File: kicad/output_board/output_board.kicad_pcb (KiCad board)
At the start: 2 copper layers, 0 parts

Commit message: add draft output board
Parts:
- added C1: 22uF, Capacitor_SMD:C_0805_2012Metric, F.Cu at (121.0, 82.0)
- added C10: 220uF, Capacitor_THT:CP_Radial_D8.0mm_P3.50mm, F.Cu at (135.4, 80.0)
- added C11: 100nF, Capacitor_SMD:C_0603_1608Metric, F.Cu at (138.5, 77.0)
- added C12: 220uF, Capacitor_THT:CP_Radial_D8.0mm_P3.50mm, F.Cu at (135.4, 91.1)
- added C13: 100nF, Capacitor_SMD:C_0603_1608Metric, F.Cu at (138.5, 88.1)
- added C14: 220uF, Capacitor_THT:CP_Radial_D8.0mm_P3.50mm, F.Cu at (135.4, 113.4)
- added C15: 100nF, Capacitor_SMD:C_0603_1608Metric, F.Cu at (138.5, 110.4)
- added C2: 22uF, Capacitor_SMD:C_0805_2012Metric, F.Cu at (124.0, 82.0)
- added C3: 22uF, Capacitor_SMD:C_0805_2012Metric, F.Cu at (127.1, 82.0)
- added C4: 10nF, Capacitor_SMD:C_0603_1608Metric, F.Cu at (112.5, 75.0)
- added C5: 220uF, Capacitor_THT:CP_Radial_D8.0mm_P3.50mm, F.Cu at (106.9, 91.4)
- added C6: 1uF, Capacitor_SMD:C_0603_1608Metric, F.Cu at (112.9, 102.2)
- added C7: 100nF, Capacitor_SMD:C_0603_1608Metric, F.Cu at (112.9, 104.8)
- added C8: 220uF, Capacitor_THT:CP_Radial_D8.0mm_P3.50mm, F.Cu at (135.4, 102.3)
- added C9: 100nF, Capacitor_SMD:C_0603_1608Metric, F.Cu at (138.4, 99.2)
- added D1: SS34, Diode_SMD:D_SMA, F.Cu at (117.2, 75.9)
- added D2: SMAJ13A, Diode_SMD:D_SMA, F.Cu at (148.2, 102.7)
- added D3: BAV23CL, Package_TO_SOT_SMD:SOT-23-3, F.Cu at (153.9, 102.7)
- added D4: SMAJ13A, Diode_SMD:D_SMA, F.Cu at (148.2, 80.4)
- added D5: BAV23CL, Package_TO_SOT_SMD:SOT-23-3, F.Cu at (153.9, 80.4)
- added D6: SMAJ13A, Diode_SMD:D_SMA, F.Cu at (148.2, 91.5)
- added D7: BAV23CL, Package_TO_SOT_SMD:SOT-23-3, F.Cu at (153.9, 91.5)
- added D8: SMAJ13A, Diode_SMD:D_SMA, F.Cu at (148.2, 113.8)
- added D9: BAV23CL, Package_TO_SOT_SMD:SOT-23-3, F.Cu at (153.9, 113.8)
- added FID1: Fiducial, Fiducial:Fiducial_1mm_Mask2mm, F.Cu at (123.3, 74.5)
- added FID2: Fiducial, Fiducial:Fiducial_1mm_Mask2mm, F.Cu at (210.4, 94.2)
- added FID3: Fiducial, Fiducial:Fiducial_1mm_Mask2mm, F.Cu at (105.5, 112.0)
- added H1: MountingHole, MountingHole:MountingHole_2.2mm_M2, F.Cu at (184.3, 74.5)
- added H2: MountingHole, MountingHole:MountingHole_2.2mm_M2, F.Cu at (105.5, 117.7)
- added J1: DRV_PWR, Connector_PinHeader_2.54mm:PinHeader_1x05_P2.54mm_Vertical, B.Cu at (137.3, 74.5)
- added J2: DRV, Connector_PinHeader_2.54mm:PinHeader_2x08_P2.54mm_Vertical, B.Cu at (124.6, 117.7)
- added J3: CH_OUT, Connector_PinSocket_2.54mm:PinSocket_1x12_P2.54mm_Vertical, B.Cu at (170.3, 117.7)
- added L1: 15uH, SaawLib:L_CJIANG_FXL0630, F.Cu at (106.9, 76.7)
- added Q1: IRF9Z24NPBF, Package_TO_SOT_THT:TO-220-3_Vertical, F.Cu at (141.1, 100.4)
- added Q10: IRF9Z24NPBF, Package_TO_SOT_THT:TO-220-3_Vertical, F.Cu at (141.1, 111.6)
- added Q11: AO3400A, Package_TO_SOT_SMD:SOT-23, F.Cu at (154.0, 117.4)
- added Q12: AO3400A, Package_TO_SOT_SMD:SOT-23, F.Cu at (154.0, 110.2)
- added Q2: AO3400A, Package_TO_SOT_SMD:SOT-23, F.Cu at (153.9, 106.2)
- added Q3: AO3400A, Package_TO_SOT_SMD:SOT-23, F.Cu at (153.9, 99.1)
- added Q4: IRF9Z24NPBF, Package_TO_SOT_THT:TO-220-3_Vertical, F.Cu at (141.1, 78.2)
- added Q5: AO3400A, Package_TO_SOT_SMD:SOT-23, F.Cu at (154.0, 84.0)
- added Q6: AO3400A, Package_TO_SOT_SMD:SOT-23, F.Cu at (154.0, 76.9)
- added Q7: IRF9Z24NPBF, Package_TO_SOT_THT:TO-220-3_Vertical, F.Cu at (141.1, 89.3)
- added Q8: AO3400A, Package_TO_SOT_SMD:SOT-23, F.Cu at (154.0, 95.1)
- added Q9: AO3400A, Package_TO_SOT_SMD:SOT-23, F.Cu at (154.0, 88.0)
- added R1: 100k, Resistor_SMD:R_0603_1608Metric, F.Cu at (121.4, 100.8)
- added R10: 100k, Resistor_SMD:R_0603_1608Metric, F.Cu at (148.0, 99.1)
- added R11: 100, Resistor_SMD:R_0603_1608Metric, F.Cu at (150.6, 99.1)
- added R12: 10k, Resistor_SMD:R_0603_1608Metric, F.Cu at (109.0, 104.8)
- added R13: 10k, Resistor_SMD:R_0603_1608Metric, F.Cu at (109.0, 102.2)
- added R14: 2k, Resistor_SMD:R_0603_1608Metric, F.Cu at (138.5, 84.5)
- added R15: 1k, Resistor_SMD:R_0603_1608Metric, F.Cu at (135.4, 85.1)
- added R16: 100k, Resistor_SMD:R_0603_1608Metric, F.Cu at (148.0, 84.0)
- added R17: 100, Resistor_SMD:R_0603_1608Metric, F.Cu at (150.6, 84.0)
- added R18: 100k, Resistor_SMD:R_0603_1608Metric, F.Cu at (148.0, 76.9)
- added R19: 100, Resistor_SMD:R_0603_1608Metric, F.Cu at (150.6, 76.9)
- added R2: 10k, Resistor_SMD:R_0603_1608Metric, F.Cu at (109.7, 86.2)
- added R20: 10k, Resistor_SMD:R_0603_1608Metric, F.Cu at (110.2, 115.8)
- added R21: 10k, Resistor_SMD:R_0603_1608Metric, F.Cu at (110.2, 118.3)
- added R22: 2k, Resistor_SMD:R_0603_1608Metric, F.Cu at (138.5, 95.6)
- added R23: 1k, Resistor_SMD:R_0603_1608Metric, F.Cu at (135.4, 96.2)
- added R24: 100k, Resistor_SMD:R_0603_1608Metric, F.Cu at (148.0, 95.1)
- added R25: 100, Resistor_SMD:R_0603_1608Metric, F.Cu at (150.6, 95.1)
- added R26: 100k, Resistor_SMD:R_0603_1608Metric, F.Cu at (148.0, 88.0)
- added R27: 100, Resistor_SMD:R_0603_1608Metric, F.Cu at (150.6, 88.0)
- added R28: 10k, Resistor_SMD:R_0603_1608Metric, F.Cu at (115.7, 118.3)
- added R29: 10k, Resistor_SMD:R_0603_1608Metric, F.Cu at (115.7, 115.8)
- added R3: 1.5k, Resistor_SMD:R_0603_1608Metric, F.Cu at (113.3, 86.2)
- added R30: 2k, Resistor_SMD:R_0603_1608Metric, F.Cu at (138.5, 117.9)
- added R31: 1k, Resistor_SMD:R_0603_1608Metric, F.Cu at (135.4, 118.5)
- added R32: 100k, Resistor_SMD:R_0603_1608Metric, F.Cu at (148.0, 117.4)
- added R33: 100, Resistor_SMD:R_0603_1608Metric, F.Cu at (150.6, 117.3)
- added R34: 100k, Resistor_SMD:R_0603_1608Metric, F.Cu at (148.0, 110.2)
- added R35: 100, Resistor_SMD:R_0603_1608Metric, F.Cu at (150.6, 110.2)
- added R4: 10k, Resistor_SMD:R_0603_1608Metric, F.Cu at (116.7, 102.2)
- added R5: 10k, Resistor_SMD:R_0603_1608Metric, F.Cu at (116.7, 104.8)
- added R6: 2k, Resistor_SMD:R_0603_1608Metric, F.Cu at (138.4, 106.7)
- added R7: 1k, Resistor_SMD:R_0603_1608Metric, F.Cu at (135.3, 107.4)
- added R8: 100k, Resistor_SMD:R_0603_1608Metric, F.Cu at (148.0, 106.2)
- added R9: 100, Resistor_SMD:R_0603_1608Metric, F.Cu at (150.6, 106.2)
- added T1: 42TL004/42TU200, SaawLib:42TL_TU, F.Cu at (170.3, 105.0)
- added T2: 42TL004/42TU200, SaawLib:42TL_TU, F.Cu at (170.3, 83.4)
- added T3: 42TL004/42TU200, SaawLib:42TL_TU, F.Cu at (198.2, 83.4)
- added T4: 42TL004/42TU200, SaawLib:42TL_TU, F.Cu at (198.2, 105.0)
- added TP1: 9V2, TestPoint:TestPoint_Pad_D1.0mm, F.Cu at (104.3, 96.0)
- added U1: TPS5430DDA, Package_SO:TI_SO-PowerPAD-8_ThermalVias, F.Cu at (115.2, 81.7)
- added U2: LM324DT, Package_SO:SOIC-14_3.9x8.7mm_P1.27mm, F.Cu at (112.9, 110.2)
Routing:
- net +9V: track 0.00 -> 176.4 mm
- net Net-(Q10-D): track 0.00 -> 75.8 mm
- net Net-(Q7-D): track 0.00 -> 74.8 mm
- net Net-(D9A-A): track 0.00 -> 62.4 mm
- net Net-(D7A-A): track 0.00 -> 61.6 mm
- net Net-(Q12-D): track 0.00 -> 56.3 mm
- net Net-(Q9-D): track 0.00 -> 55.3 mm
- net Net-(R13-Pad1): track 0.00 -> 47.5 mm, vias 0 -> 2
- net Net-(R21-Pad1): track 0.00 -> 40.9 mm, vias 0 -> 2
- net /CH2_GA: track 0.00 -> 40.8 mm
- net /Channel 3/OUTB: track 0.00 -> 40.0 mm
- net /Channel 2/OUTA: track 0.00 -> 39.9 mm
- net /CH2_GB: track 0.00 -> 36.7 mm
- net /CH3_GA: track 0.00 -> 35.7 mm
- net /Channel 3/OUTM: track 0.00 -> 34.1 mm
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- added copper zone on F.Cu, net +9V
- added copper zone on B.Cu, net /PGND
- added copper zone on F.Cu, net /PGND
- added copper zone on B.Cu, net GND
- added copper zone on F.Cu, net GND
- added copper zone on F.Cu, net Net-(D1-K)
- added copper zone on F.Cu, net VIN
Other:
- board outline added: 109.2 x 48.3 mm

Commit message: cleanup
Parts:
- added H3: MountingHole, MountingHole:MountingHole_2.2mm_M2, F.Cu at (209.7, 117.7)
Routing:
- net GND: track 2.96 -> 6.33 mm, vias 33 -> 37
- net /DRV_EN: track 23.1 -> 22.4 mm
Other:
- board text added: "JLCJLCJLCJLC"

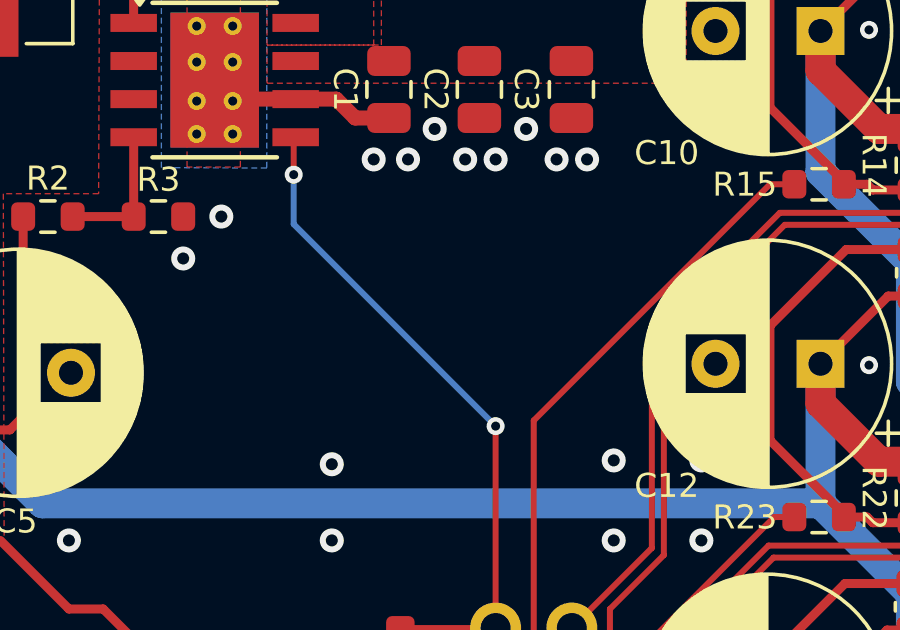
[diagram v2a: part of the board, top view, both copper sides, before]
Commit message: add silkscreen board info
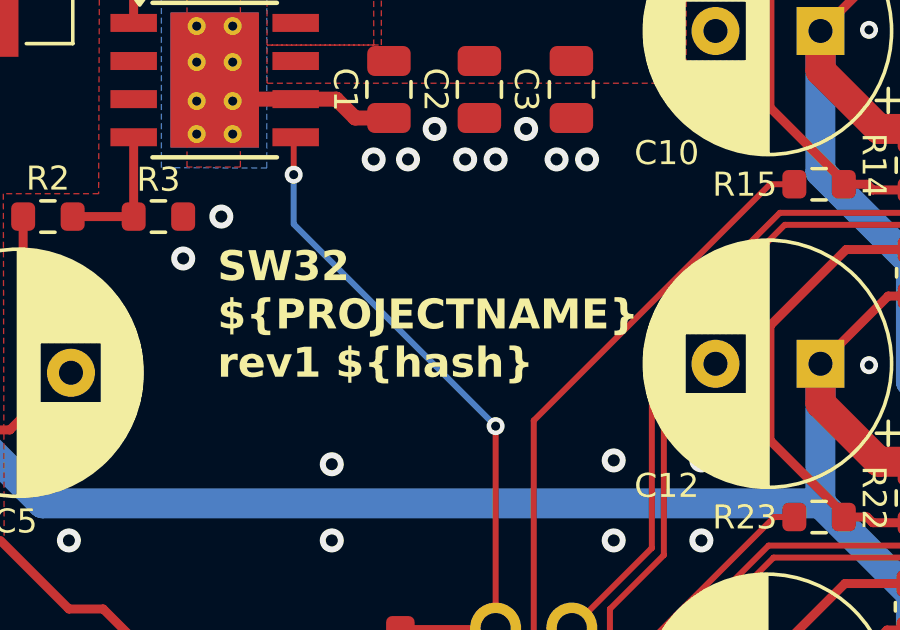
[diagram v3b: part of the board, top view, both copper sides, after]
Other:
- board text added: "SW32 ${PROJECTNAME} rev${REVISION} ${hash}"
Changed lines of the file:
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@@
+		)
+	)
+	(gr_text "SW32\n${PROJECTNAME}\nrev${REVISION} ${hash}"
+		(locked yes)
+		(at 115.316032 91.674197 0)
+		(layer "F.SilkS")
+		(effects
+			(font
+				(size 1 1)
+				(thickness 0.15)
+				(bold yes)
+			)
+			(justify left bottom)
 		)
 	)
